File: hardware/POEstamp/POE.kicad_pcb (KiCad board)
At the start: 2 copper layers, 70 x 40 mm, 61 parts, among them J1 0813-1X1T-57-F, P3 GND, P4 +5V, P5 CONN_01X05, P6 5Vout, P7 GNDout, Q1 SI3440DV, NFET, Q2 2N7002, Q3 MMBTA42, T1 PA1134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

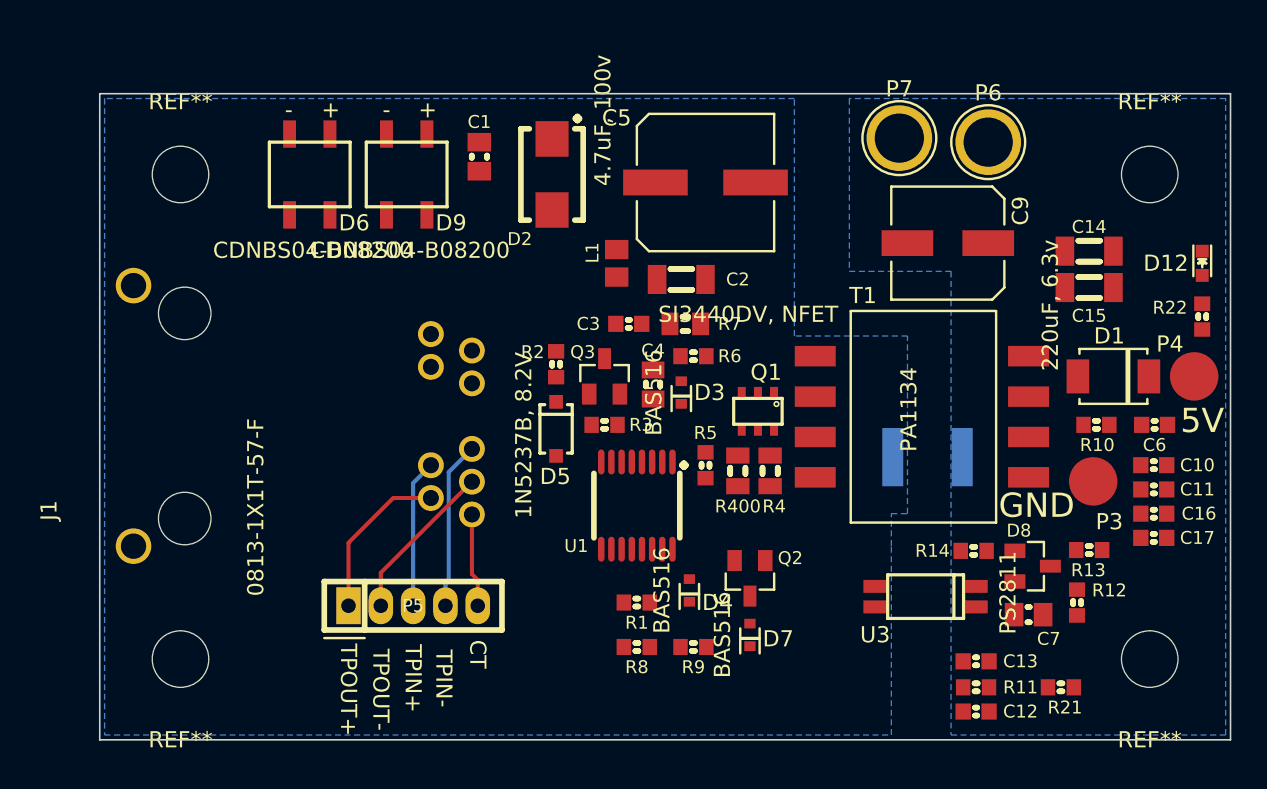
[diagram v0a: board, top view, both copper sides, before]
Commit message: Almost all traces routed sans ground connections on the ethernet side.
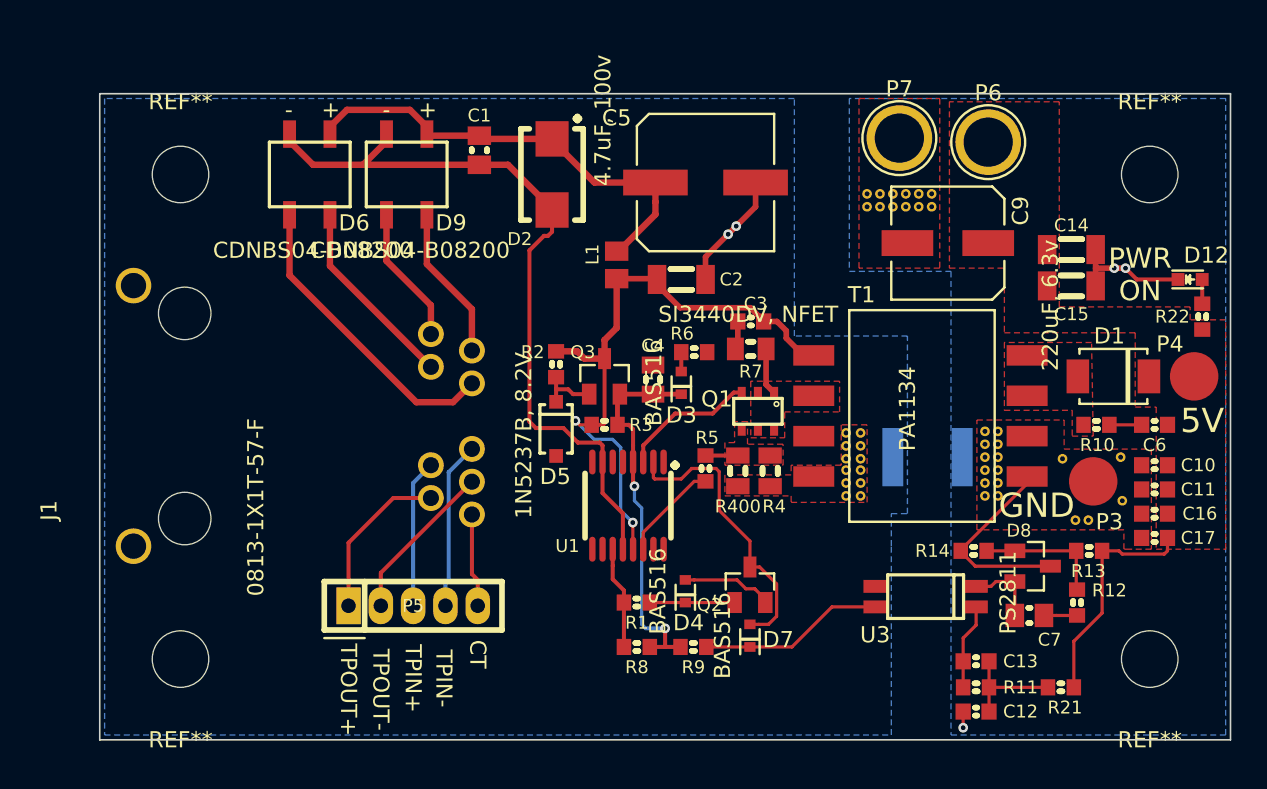
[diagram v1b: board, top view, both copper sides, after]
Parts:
- added REF**111: VIA-0.6mm, rfid:VIA-0.6mm, F.Cu at (116.2, 55.0)
- added REF**111: VIA-0.6mm, rfid:VIA-0.6mm, F.Cu at (116.2, 57.3)
- added REF**11111: VIA-0.6mm, rfid:VIA-0.6mm, F.Cu at (117.5, 40.2)
- added REF**11111: VIA-0.6mm, rfid:VIA-0.6mm, F.Cu at (119.1, 40.2)
- added REF**11111: VIA-0.6mm, rfid:VIA-0.6mm, F.Cu at (120.7, 40.2)
- added REF**11111: VIA-0.6mm, rfid:VIA-0.6mm, F.Cu at (124.8, 54.9)
- added REF**11112: VIA-0.6mm, rfid:VIA-0.6mm, F.Cu at (117.5, 41.0)
- added REF**11112: VIA-0.6mm, rfid:VIA-0.6mm, F.Cu at (119.1, 41.0)
- added REF**11112: VIA-0.6mm, rfid:VIA-0.6mm, F.Cu at (120.7, 41.0)
- added REF**11112: VIA-0.6mm, rfid:VIA-0.6mm, F.Cu at (124.8, 55.7)
- added REF**11113: VIA-0.6mm, rfid:VIA-0.6mm, F.Cu at (124.8, 56.5)
- added REF**11114: VIA-0.6mm, rfid:VIA-0.6mm, F.Cu at (124.8, 57.3)
- added REF**11115: VIA-0.6mm, rfid:VIA-0.6mm, F.Cu at (124.8, 58.1)
- added REF**11116: VIA-0.6mm, rfid:VIA-0.6mm, F.Cu at (124.8, 58.9)
- added REF**11121: VIA-0.6mm, rfid:VIA-0.6mm, F.Cu at (118.3, 40.2)
- added REF**11121: VIA-0.6mm, rfid:VIA-0.6mm, F.Cu at (119.9, 40.2)
- added REF**11121: VIA-0.6mm, rfid:VIA-0.6mm, F.Cu at (121.5, 40.2)
- added REF**11121: VIA-0.6mm, rfid:VIA-0.6mm, F.Cu at (130.4, 60.4)
- added REF**11121: VIA-0.6mm, rfid:VIA-0.6mm, F.Cu at (131.2, 60.4)
- added REF**11121: VIA-0.6mm, rfid:VIA-0.6mm, F.Cu at (133.3, 59.2)
- added REF**11121: VIA-0.6mm, rfid:VIA-0.6mm, F.Cu at (133.2, 56.5)
- added REF**11121: VIA-0.6mm, rfid:VIA-0.6mm, F.Cu at (129.6, 56.6)
- added REF**11121: VIA-0.6mm, rfid:VIA-0.6mm, F.Cu at (125.6, 54.9)
- added REF**11122: VIA-0.6mm, rfid:VIA-0.6mm, F.Cu at (118.3, 41.0)
- added REF**11122: VIA-0.6mm, rfid:VIA-0.6mm, F.Cu at (119.9, 41.0)
- added REF**11122: VIA-0.6mm, rfid:VIA-0.6mm, F.Cu at (121.5, 41.0)
- added REF**11122: VIA-0.6mm, rfid:VIA-0.6mm, F.Cu at (125.6, 55.7)
- added REF**11123: VIA-0.6mm, rfid:VIA-0.6mm, F.Cu at (125.6, 56.5)
- added REF**11124: VIA-0.6mm, rfid:VIA-0.6mm, F.Cu at (125.6, 57.3)
- added REF**11125: VIA-0.6mm, rfid:VIA-0.6mm, F.Cu at (125.6, 58.1)
- added REF**11126: VIA-0.6mm, rfid:VIA-0.6mm, F.Cu at (125.6, 58.9)
- added REF**112: VIA-0.6mm, rfid:VIA-0.6mm, F.Cu at (116.2, 55.8)
- added REF**112: VIA-0.6mm, rfid:VIA-0.6mm, F.Cu at (116.2, 58.1)
- added REF**113: VIA-0.6mm, rfid:VIA-0.6mm, F.Cu at (116.2, 56.6)
- added REF**113: VIA-0.6mm, rfid:VIA-0.6mm, F.Cu at (116.2, 58.9)
- added REF**121: VIA-0.6mm, rfid:VIA-0.6mm, F.Cu at (117.1, 55.0)
- added REF**121: VIA-0.6mm, rfid:VIA-0.6mm, F.Cu at (117.1, 57.3)
- added REF**122: VIA-0.6mm, rfid:VIA-0.6mm, F.Cu at (117.1, 55.8)
- added REF**122: VIA-0.6mm, rfid:VIA-0.6mm, F.Cu at (117.1, 58.1)
- added REF**123: VIA-0.6mm, rfid:VIA-0.6mm, F.Cu at (117.1, 56.6)
- added REF**123: VIA-0.6mm, rfid:VIA-0.6mm, F.Cu at (117.1, 58.9)
- moved C3 7.55 mm to (110.3, 48.1), turned to 180 degrees
- moved R7 4.34 mm to (110.3, 49.8)
- moved D12 1.25 mm to (137.5, 45.5), turned to 0 degrees
- moved C14 1.10 mm to (130.2, 43.6)
- moved C15 1.10 mm to (130.2, 45.9)
- moved D3 0.60 mm to (106.0, 51.9)
- moved U1 0.55 mm to (102.7, 59.5)
- moved Q2 0.40 mm to (110.2, 64.4), turned to 90 degrees
- moved C1 0.40 mm to (93.5, 37.5)
- moved C4 0.30 mm to (104.2, 51.7)
- moved D4 0.25 mm to (106.2, 64.8)
- moved R6 0.25 mm to (106.8, 50.0)
- moved R5 0.20 mm to (107.5, 57.2)
- moved T1 0.10 mm to (114.2, 50.2)
- moved L1 0.10 mm to (102.0, 44.6)
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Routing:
- net Net-(C1-Pad2): track 0.00 -> 46.9 mm
- net Net-(C2-Pad1): track 0.00 -> 39.1 mm, vias 0 -> 2
- net Net-(C1-Pad1): track 0.00 -> 28.5 mm
- net /PVcc: track 0.00 -> 23.7 mm, vias 0 -> 2
- net GND: track 0.00 -> 20.9 mm, vias 0 -> 3
- net /Ethernet+: track 0.00 -> 18.8 mm
- net /Ith/Run: track 0.00 -> 18.1 mm
- net 5VPoE: track 0.00 -> 14.5 mm
- net GNDA: track 0.00 -> 13.2 mm, vias 0 -> 2
- net /Ethernet-: track 0.00 -> 12.0 mm
- net Net-(D7-Pad2): track 0.00 -> 11.5 mm
- net /EthernetSpare-: track 0.00 -> 9.56 mm
- net /EthernetSpare+: track 0.00 -> 8.52 mm
- net /NGate: track 0.00 -> 8.48 mm
- net Net-(D8-Pad1): track 0.00 -> 7.97 mm
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- added copper zone on F.Cu, net 5VPoE
- added copper zone on F.Cu, net GND
- added copper zone on F.Cu, net GNDA
- added copper zone on F.Cu, net Net-(D1-Pad1)
- added copper zone on F.Cu, net Net-(Q1-Pad1)
- added copper zone on F.Cu, net Net-(Q1-Pad4)
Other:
- board text added: "PWR ON"

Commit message: Completed routing of POEStamp.
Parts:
- added REF**111: VIA-0.6mm, rfid:VIA-0.6mm, F.Cu at (108.0, 61.9)
- added REF**111: VIA-0.6mm, rfid:VIA-0.6mm, F.Cu at (106.2, 61.9)
- added REF**111: VIA-0.6mm, rfid:VIA-0.6mm, F.Cu at (106.2, 60.3)
- added REF**111: VIA-0.6mm, rfid:VIA-0.6mm, F.Cu at (105.5, 55.1)
- added REF**111: VIA-0.6mm, rfid:VIA-0.6mm, F.Cu at (109.9, 41.8)
- added REF**111: VIA-0.6mm, rfid:VIA-0.6mm, F.Cu at (108.2, 41.8)
- added REF**111: VIA-0.6mm, rfid:VIA-0.6mm, F.Cu at (106.4, 41.8)
- added REF**111: VIA-0.6mm, rfid:VIA-0.6mm, F.Cu at (103.6, 47.8)
- added REF**112: VIA-0.6mm, rfid:VIA-0.6mm, F.Cu at (108.0, 62.7)
- added REF**112: VIA-0.6mm, rfid:VIA-0.6mm, F.Cu at (106.2, 62.7)
- added REF**112: VIA-0.6mm, rfid:VIA-0.6mm, F.Cu at (106.2, 61.1)
- added REF**112: VIA-0.6mm, rfid:VIA-0.6mm, F.Cu at (105.5, 55.9)
- added REF**112: VIA-0.6mm, rfid:VIA-0.6mm, F.Cu at (109.9, 42.6)
- added REF**112: VIA-0.6mm, rfid:VIA-0.6mm, F.Cu at (108.2, 42.6)
- added REF**112: VIA-0.6mm, rfid:VIA-0.6mm, F.Cu at (106.4, 42.6)
- added REF**112: VIA-0.6mm, rfid:VIA-0.6mm, F.Cu at (103.6, 48.6)
- added REF**121: VIA-0.6mm, rfid:VIA-0.6mm, F.Cu at (99.6, 57.6)
- added REF**121: VIA-0.6mm, rfid:VIA-0.6mm, F.Cu at (104.5, 47.8)
- added REF**121: VIA-0.6mm, rfid:VIA-0.6mm, F.Cu at (100.1, 63.8)
- added REF**121: VIA-0.6mm, rfid:VIA-0.6mm, F.Cu at (108.9, 61.9)
- added REF**121: VIA-0.6mm, rfid:VIA-0.6mm, F.Cu at (107.1, 61.9)
- added REF**121: VIA-0.6mm, rfid:VIA-0.6mm, F.Cu at (107.1, 60.3)
- added REF**121: VIA-0.6mm, rfid:VIA-0.6mm, F.Cu at (106.4, 55.1)
- added REF**121: VIA-0.6mm, rfid:VIA-0.6mm, F.Cu at (110.8, 41.8)
- added REF**121: VIA-0.6mm, rfid:VIA-0.6mm, F.Cu at (109.1, 41.8)
- added REF**121: VIA-0.6mm, rfid:VIA-0.6mm, F.Cu at (107.3, 41.8)
- added REF**122: VIA-0.6mm, rfid:VIA-0.6mm, F.Cu at (99.6, 56.8)
- added REF**122: VIA-0.6mm, rfid:VIA-0.6mm, F.Cu at (104.5, 48.6)
- added REF**122: VIA-0.6mm, rfid:VIA-0.6mm, F.Cu at (100.9, 63.8)
- added REF**122: VIA-0.6mm, rfid:VIA-0.6mm, F.Cu at (108.9, 62.7)
- added REF**122: VIA-0.6mm, rfid:VIA-0.6mm, F.Cu at (107.1, 62.7)
- added REF**122: VIA-0.6mm, rfid:VIA-0.6mm, F.Cu at (107.1, 61.1)
- added REF**122: VIA-0.6mm, rfid:VIA-0.6mm, F.Cu at (106.4, 55.9)
- added REF**122: VIA-0.6mm, rfid:VIA-0.6mm, F.Cu at (110.8, 42.6)
- added REF**122: VIA-0.6mm, rfid:VIA-0.6mm, F.Cu at (109.1, 42.6)
- added REF**122: VIA-0.6mm, rfid:VIA-0.6mm, F.Cu at (107.3, 42.6)
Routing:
- net Net-(R6-Pad2): track 0.00 -> 9.75 mm, vias 0 -> 2
- net GNDA: track 13.2 -> 5.87 mm, vias 2 -> 0

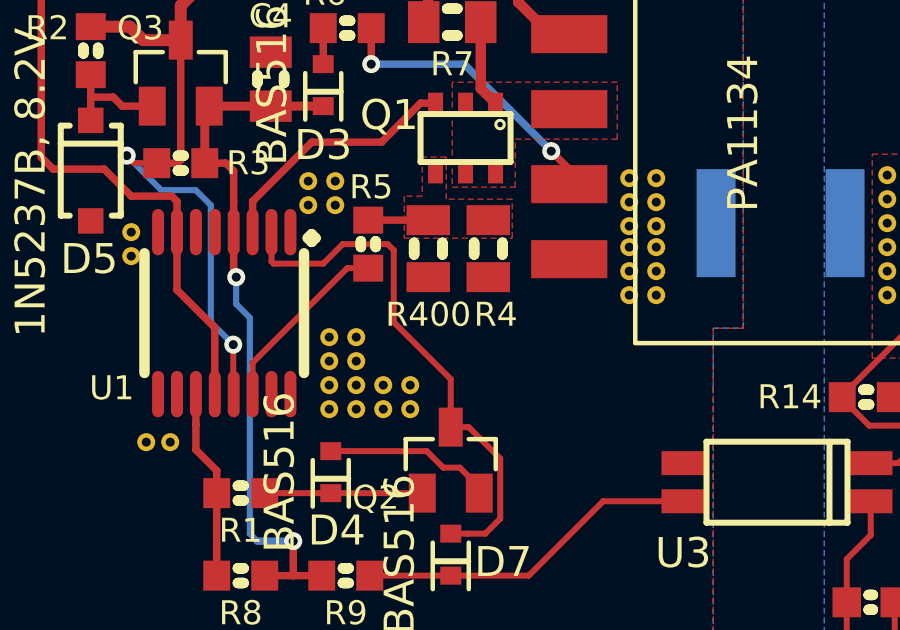
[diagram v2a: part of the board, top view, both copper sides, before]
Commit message: Added annotation silkscreen on the back as well as URl to this project, OSHW logo, etc.
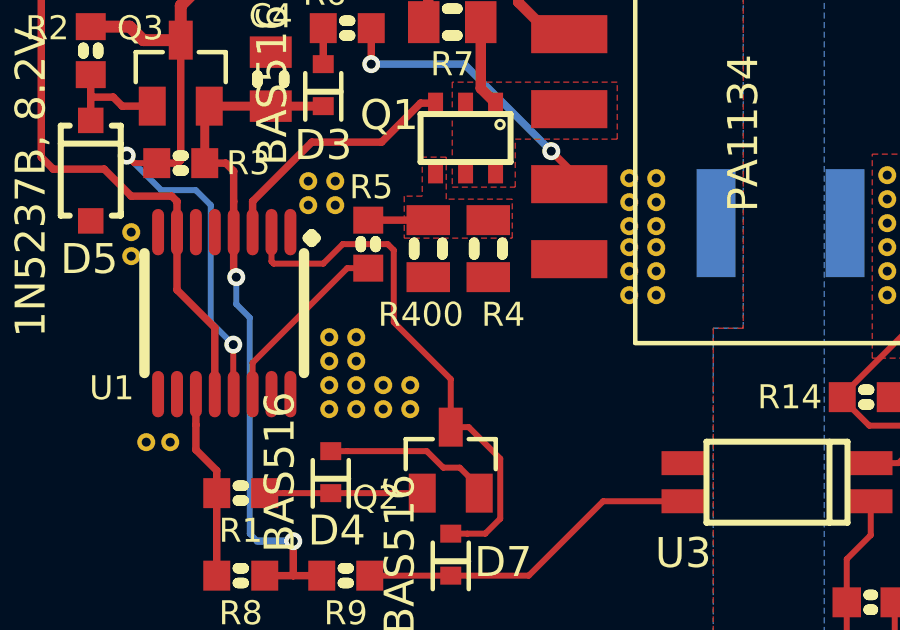
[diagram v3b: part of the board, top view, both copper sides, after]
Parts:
- added G***: LOGO, mech:OSHW-6mm, B.Cu at (80.5, 64.5)
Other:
- board text added: "+5V"
- board text added: "Bootstrap regulator"
- board text added: "Flyback switching circuit"
- board text added: "Output error amp"
- board text added: "PoE Stamp Rev 1"
- board text added: "Power good + soft start filtering"
- board text added: "Power input and filtering"
- board text added: "Power output and filtering"
- board text added: "https://github.com/reportingsjr/rfidBoard/hardware/POEstamp"
